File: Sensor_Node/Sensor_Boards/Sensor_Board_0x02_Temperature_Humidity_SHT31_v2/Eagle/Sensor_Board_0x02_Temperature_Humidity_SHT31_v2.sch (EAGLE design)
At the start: 28 parts, among them J1 M04_SMD_90, J4 ARDUINO_ISP, U1 CCS811, U2 ATMEGA328P_TQFP, Y1 8MHZ

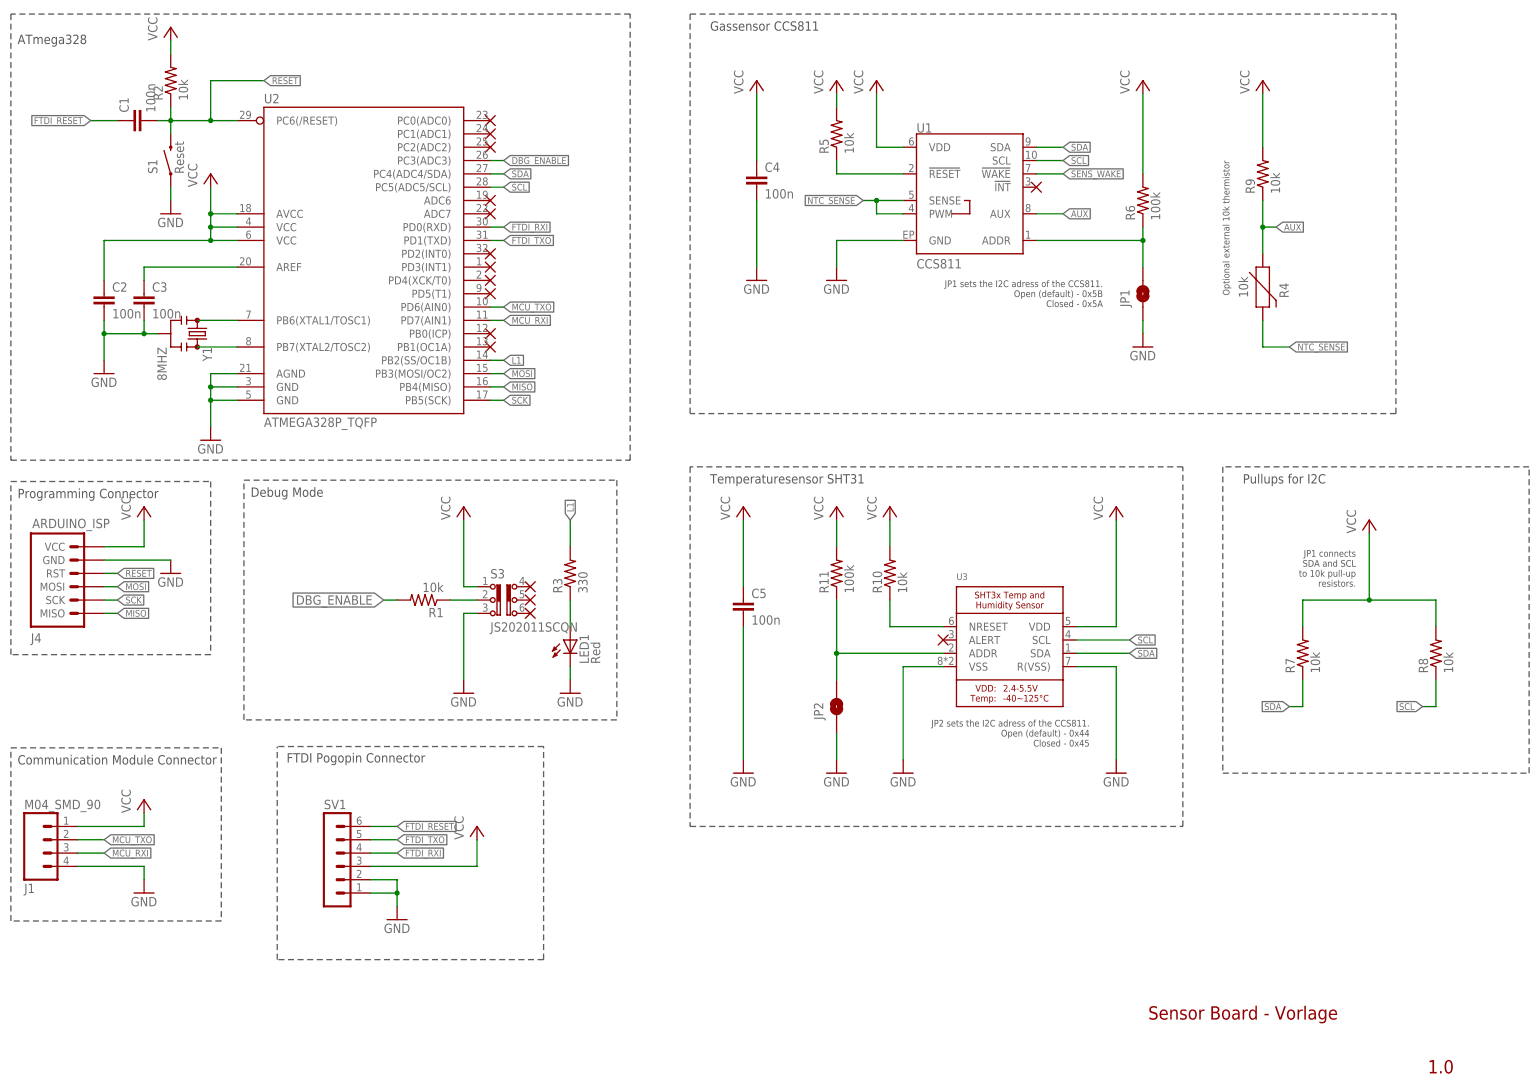
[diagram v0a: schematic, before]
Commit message: Version 2 of CO2 and SHT31 - Sensorboards
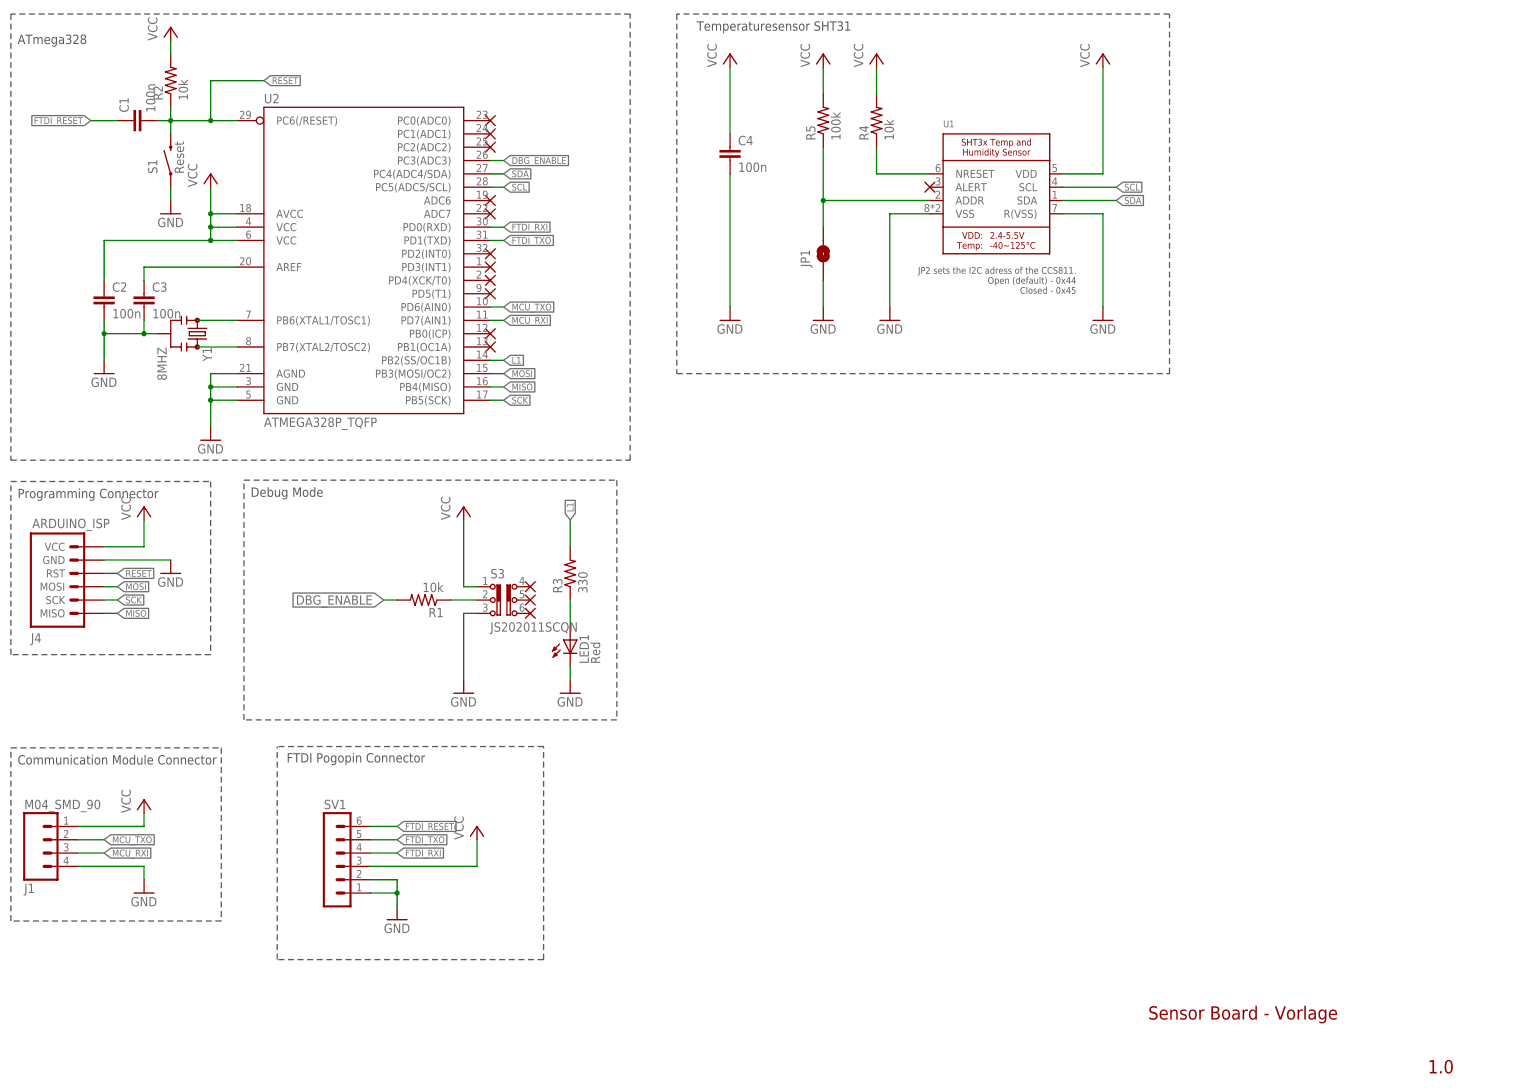
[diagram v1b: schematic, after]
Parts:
- removed C5: 100n, eagle-ltspice:C
- removed JP2: SPARKFUN-JUMPERS_JUMPER-SMT_2_NO_SILK, SparkFun_CSS811_Breakout:SPARKFUN-JUMPERS_JUMPER-SMT_2_NO_SILK
- removed R10, R7, R8, R9: 10k, SparkFun-Passives:RESISTOR0805-RES
- removed R11, R6: 100k, SparkFun-Passives:RESISTOR0805-RES
- removed U3: (no value), Adafruit SHT31 Breakout:MICROBUILDER_SHT3X
- R4: device SparkFun_CSS811_Breakout:CCS811_BREAKOUT_TEMP_NTC-THERMISTOR-0603 -> SparkFun-Passives:RESISTOR0805-RES
- R5: value 10k -> 100k
- U1: value CCS811 -> (none); device SparkFun_CSS811_Breakout:CCS811_BREAKOUT_TEMP_CCS811 -> Adafruit SHT31 Breakout:MICROBUILDER_SHT3X
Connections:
- removed net AUX: R4.1, R9.1, U1.AUX
- removed net N$7: R10.1, U3.NRESET
- removed net N$8: JP2.2, R11.1, U3.ADDR
- removed net NTC_SENSE: R4.2, U1.PWM, U1.SENSE
- removed net SENS_RES: R5.1, U1.!RESET!
- removed net SENS_WAKE: U1.!WAKE!
- new net N$5: JP1.2, R5.1, U1.ADDR
- net GND: now also U1.R(VSS), U1.VSS; no longer C5.2, JP2.1, U1.GND, U3.R(VSS), U3.VSS
- net N$4: now also R4.1, U1.NRESET; no longer JP1.2, R6.1, U1.ADDR
- net SCL: no longer R8.1, U3.SCL
- net SDA: no longer R7.1, U3.SDA
- net VCC: now also R4.2; no longer C5.1, R10.2, R11.2, R6.2, R7.2, R8.2, R9.2, U3.VDD
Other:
- note removed: "Gassensor CCS811"
- note removed: "JP1 connects SDA and SCL to 10k pull-up resistors."
- note removed: "JP1 sets the I2C adress of the CCS811. Open (default) - 0x5B Closed - 0x5A"
- note removed: "Optional external 10k thermistor"
- note removed: "Pullups for I2C"
- moved on the sheet: C4, JP1, R5
